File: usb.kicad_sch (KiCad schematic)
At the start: 55 parts, among them J901 AU-Y1008-2-BLK, J902 AU-Y1008-2-BLK, U901 USB2514B/M2, U902 AP22966DC8-7, U903 AP22966DC8-7, U904 USBLC6-2SC6, U905 USBLC6-2SC6, U906 USBLC6-2SC6, U907 USBLC6-2SC6, Y901 24 MHz

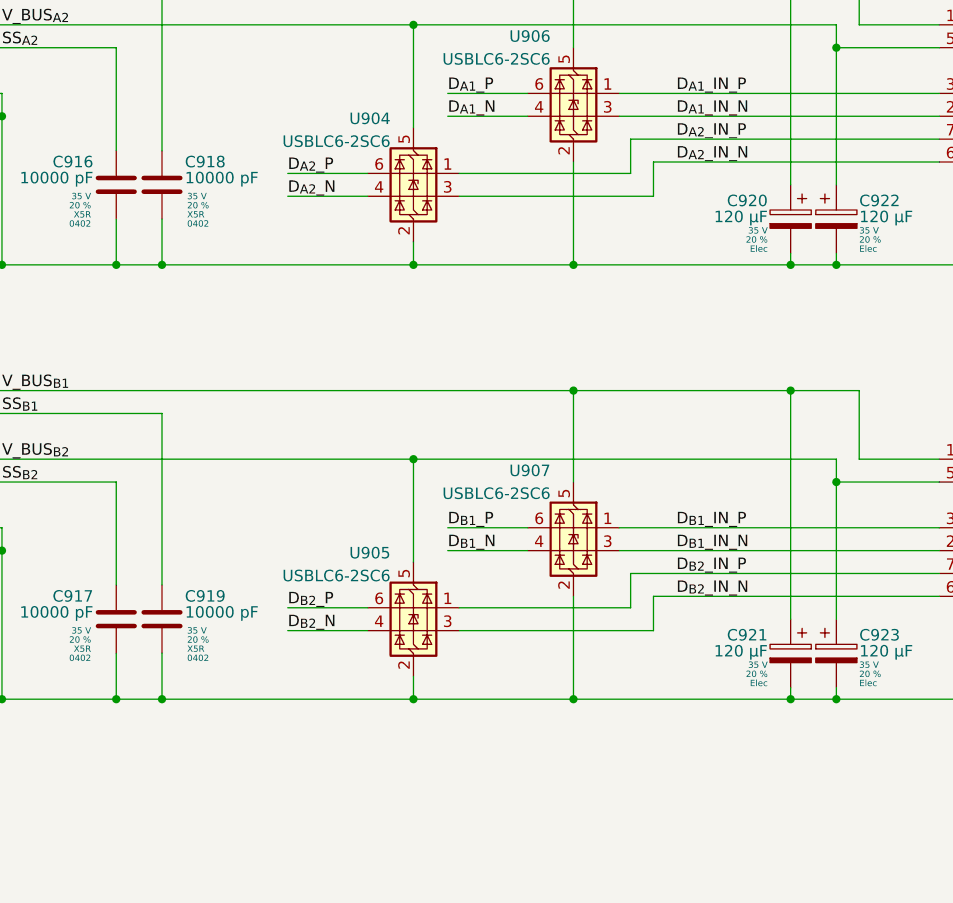
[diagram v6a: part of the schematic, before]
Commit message: Connect ESD TVS to chassis where possible, update version and date
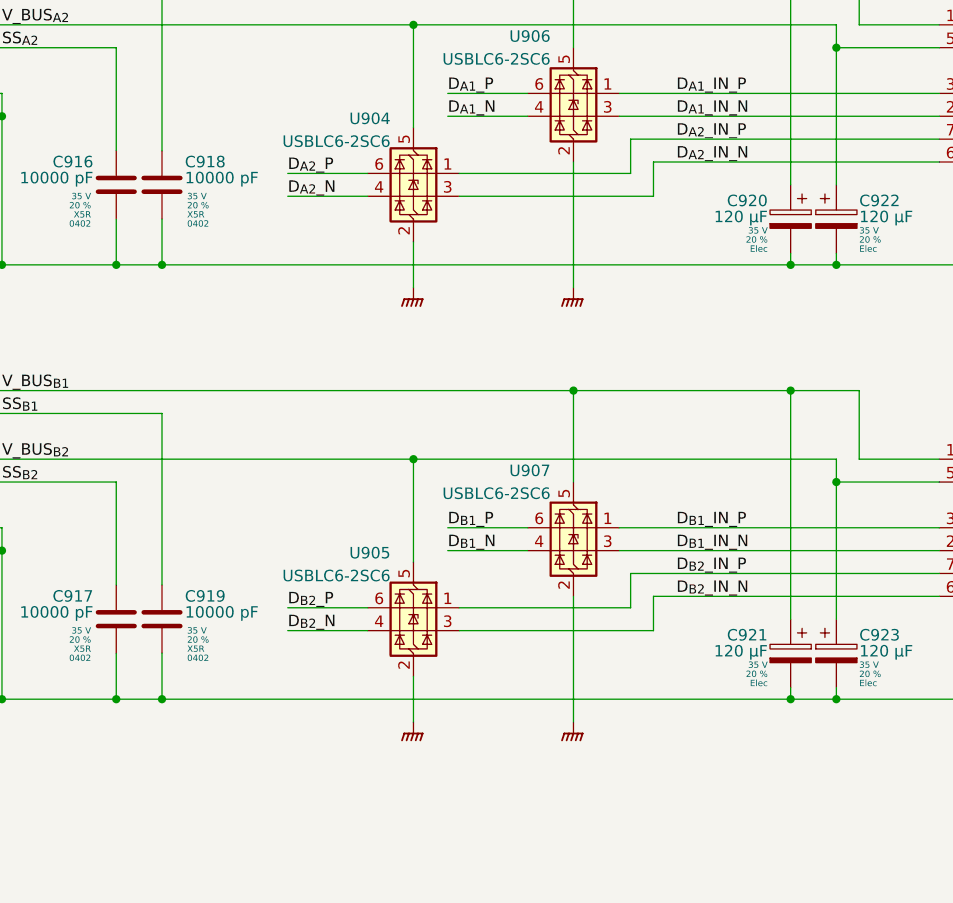
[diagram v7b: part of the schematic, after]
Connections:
- net CHASSIS: now also U904.2 (GND), U905.2 (GND), U906.2 (GND), U907.2 (GND)
- net GND: no longer U904.2 (GND), U905.2 (GND), U906.2 (GND), U907.2 (GND)

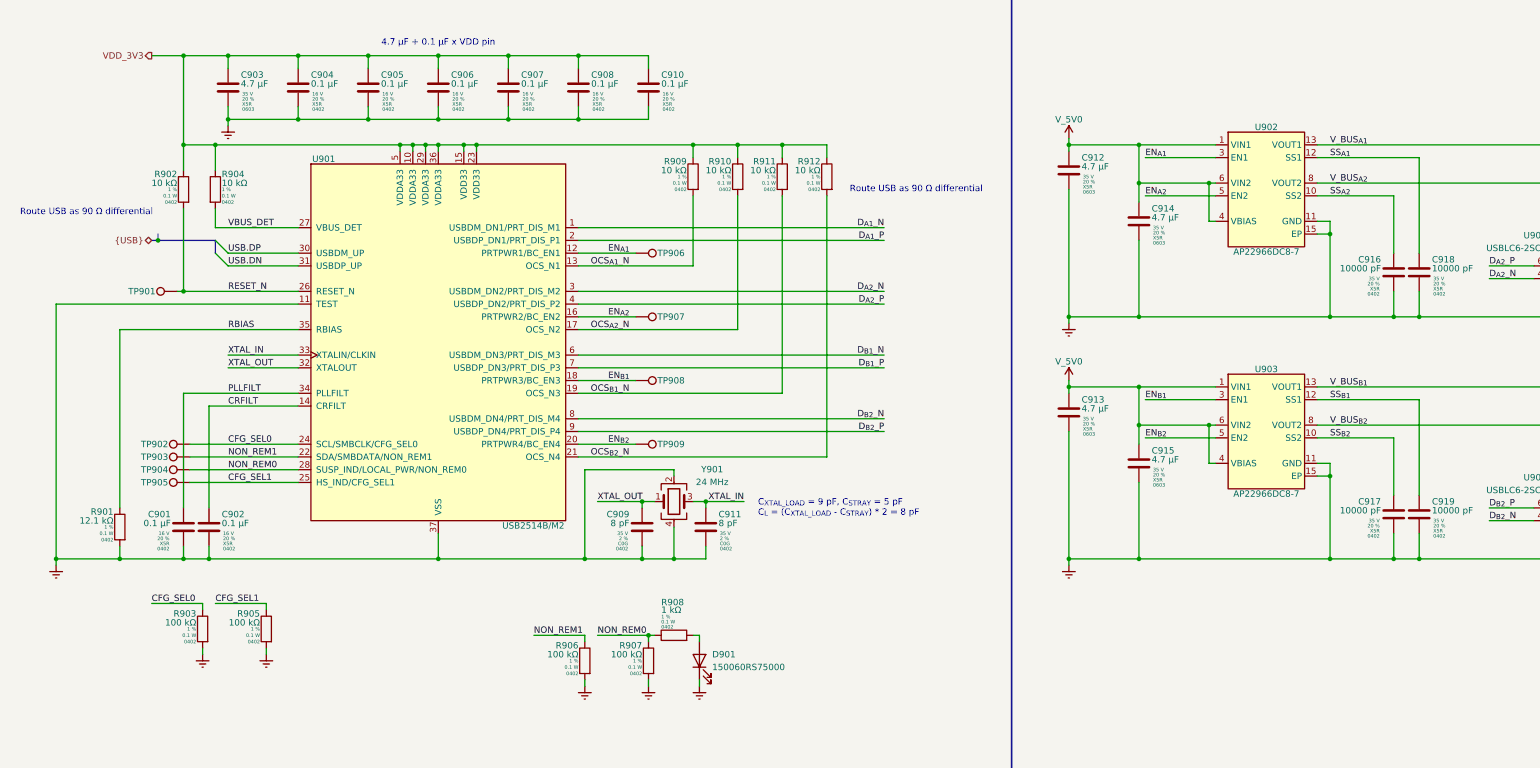
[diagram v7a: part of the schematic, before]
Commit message: 0402 -> 0201 where possible
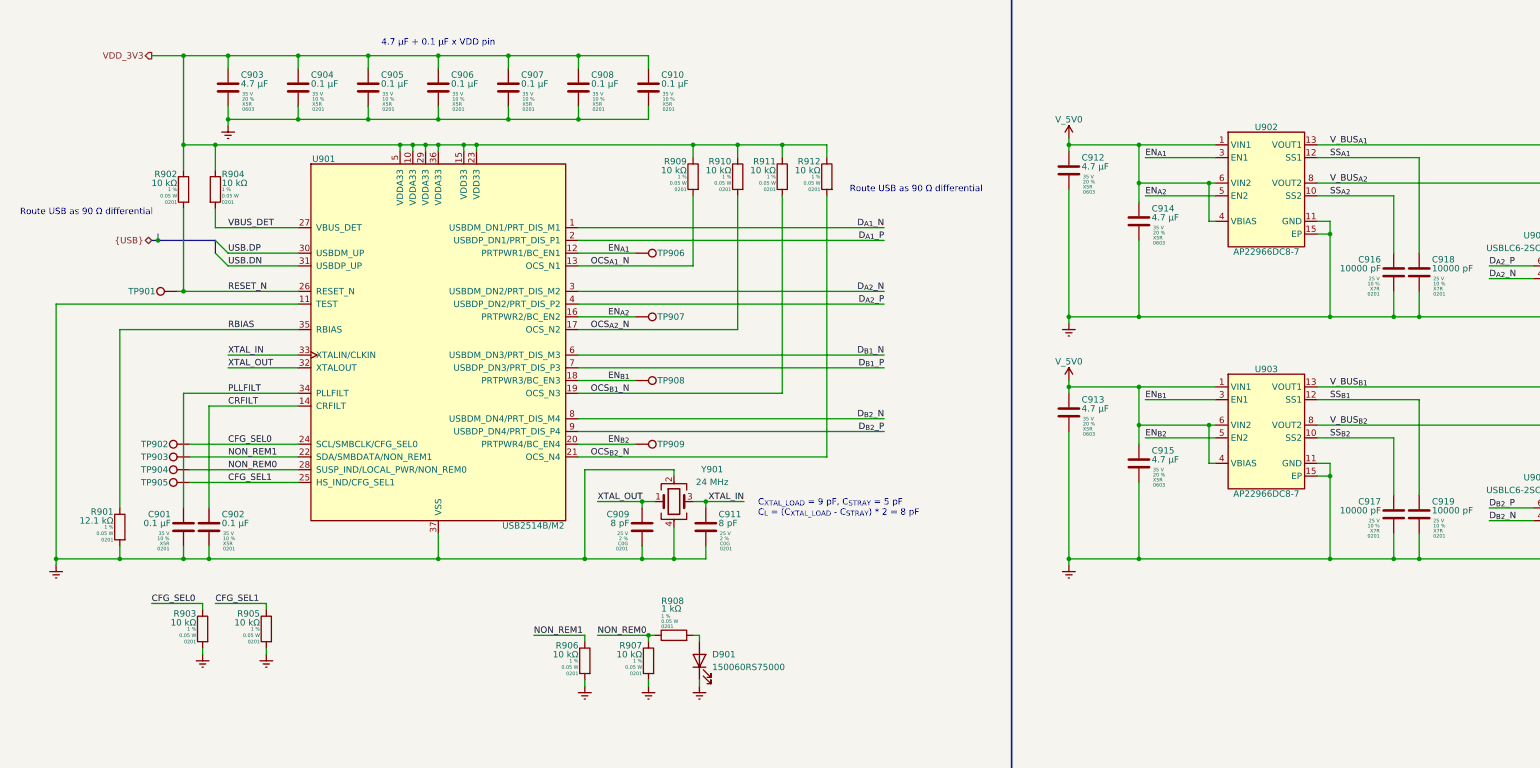
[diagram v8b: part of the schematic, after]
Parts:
- C901, C902, C904, C905, C906, C907, C908, C910: footprint perfect_footprints:C_0402_1005Metric -> Capacitor_SMD:C_0201_0603Metric; Digi-Key Part Number 490-10700-1-ND -> 490-10430-1-ND; MPN GRM155R71H104KE14D -> GRM033R6YA104KE14D; Size 0402 -> 0201; Tolerance 20 % -> 10 %; Voltage rating 16 V -> 35 V
- C909, C911: footprint perfect_footprints:C_0402_1005Metric -> Capacitor_SMD:C_0201_0603Metric; Digi-Key Part Number 490-3109-1-ND -> 490-17280-1-ND; MPN GJM1555C1H8R0CB01D -> GJM0335C1E8R0CB01D; Size 0402 -> 0201; Voltage rating 35 V -> 25 V
- C916, C917, C918, C919: footprint perfect_footprints:C_0402_1005Metric -> Capacitor_SMD:C_0201_0603Metric; Digi-Key Part Number 490-4516-1-ND -> 490-14454-1-ND; MPN GRM155R71H103KA88D -> GRM033R71E103KE14D; Size 0402 -> 0201; Temperature coefficient X5R -> X7R; Tolerance 20 % -> 10 %; Voltage rating 35 V -> 25 V
- R901: footprint perfect_footprints:R_0402_1005Metric -> Resistor_SMD:R_0201_0603Metric; Digi-Key Part Number P12.1KLCT-ND -> P122698CT-ND; MPN ERJ-2RKF1212X -> ERJ-1GNF1212C; Power rating 0.1 W -> 0.05 W; Size 0402 -> 0201
- R902, R904, R909, R910, R911, R912: footprint perfect_footprints:R_0402_1005Metric -> Resistor_SMD:R_0201_0603Metric; Digi-Key Part Number P10.0KLCT-ND -> P122414CT-ND; MPN ERJ-2RKF1002X -> ERJ-1GNF1002C; Power rating 0.1 W -> 0.05 W; Size 0402 -> 0201
- R903, R905, R906, R907: value 100 kΩ -> 10 kΩ; footprint perfect_footprints:R_0402_1005Metric -> Resistor_SMD:R_0201_0603Metric; Digi-Key Part Number P100KLCT-ND -> P122414CT-ND; MPN ERJ-2RKF1003X -> ERJ-1GNF1002C; Power rating 0.1 W -> 0.05 W; Size 0402 -> 0201
- R908: footprint perfect_footprints:R_0402_1005Metric -> Resistor_SMD:R_0201_0603Metric; Digi-Key Part Number P1.00KLCT-ND -> 10-ERJ-U01F1001CCT-ND; MPN ERJ-2RKF1001X -> ERJ-U01F1001C; Power rating 0.1 W -> 0.05 W; Size 0402 -> 0201
